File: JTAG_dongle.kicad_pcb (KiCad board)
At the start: 2 copper layers, 52.7 x 31.8 mm, 53 parts, among them J1 5V supply Enable, J2 SeggerJlink connector, J3 Conn_02x10_Odd_Even, J4 FTS-105-01-F-D

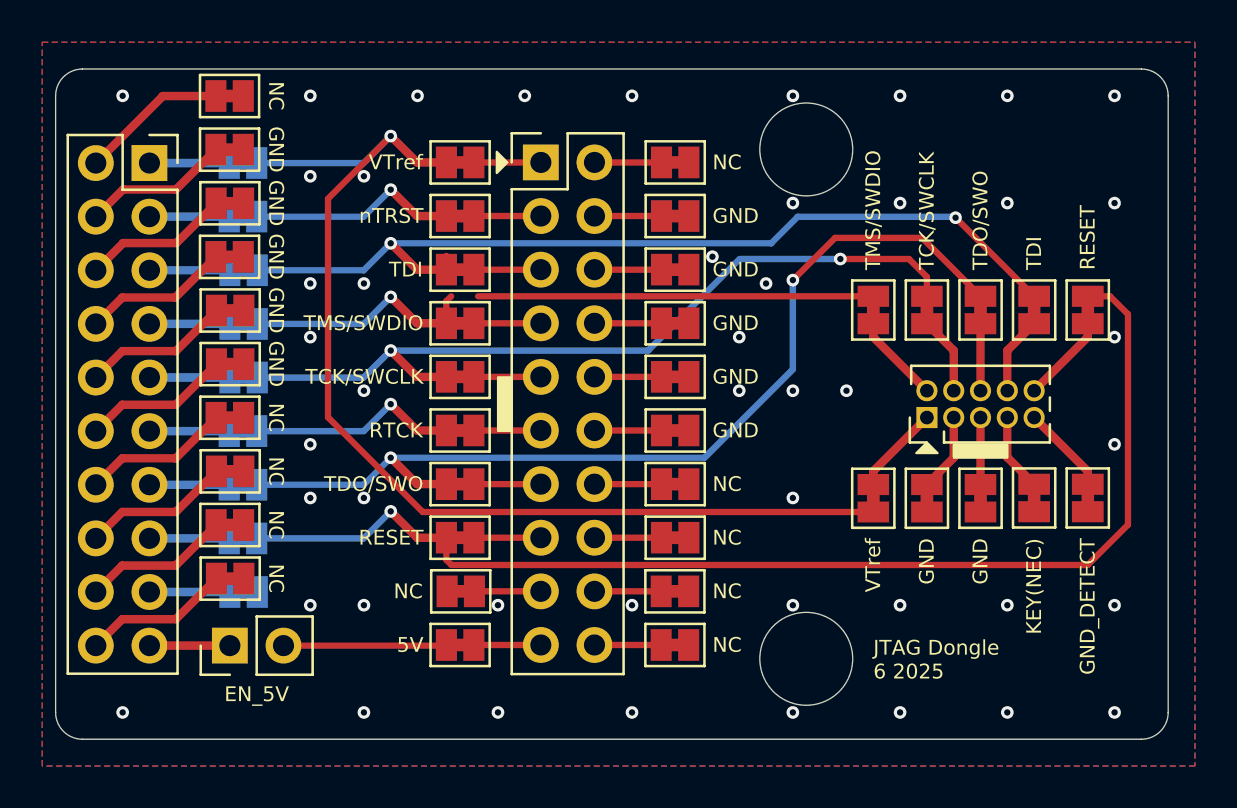
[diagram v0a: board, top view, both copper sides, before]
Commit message: fix drc erros
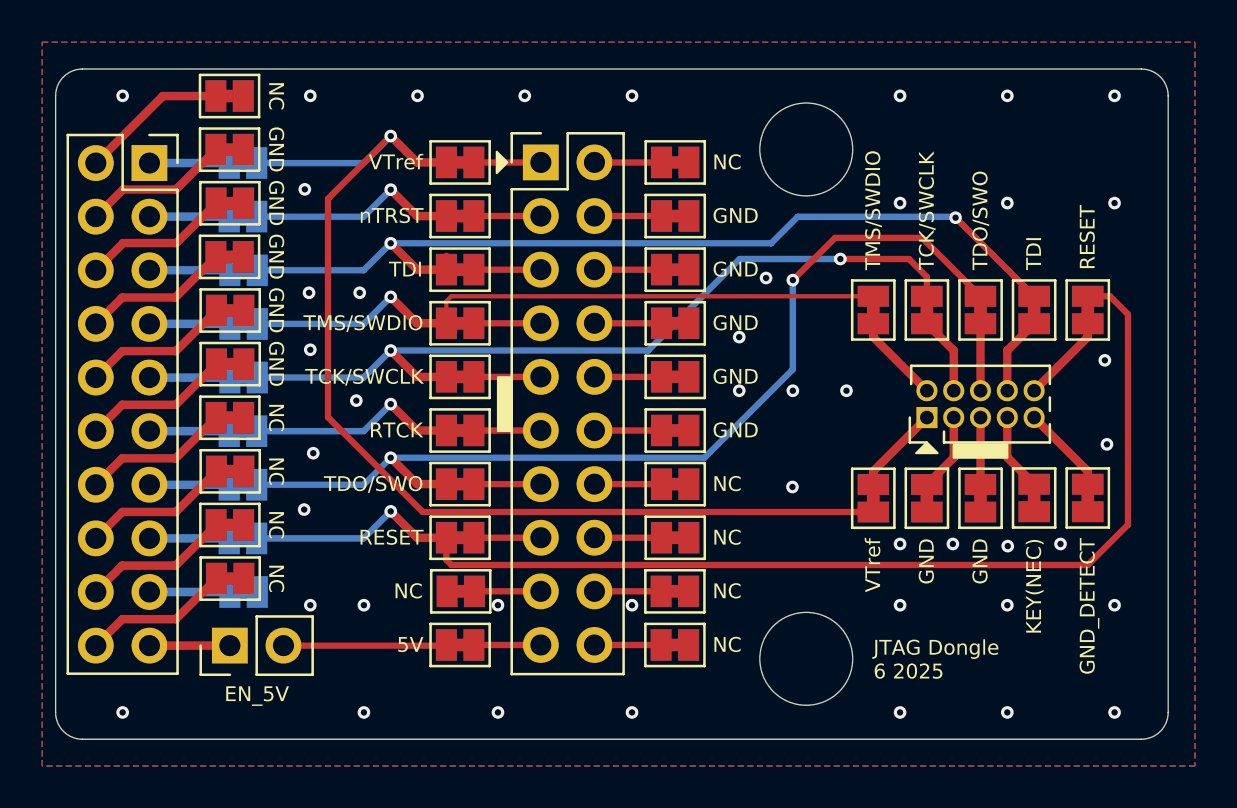
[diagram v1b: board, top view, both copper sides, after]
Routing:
- net /TMS/SWDIO: track 30.1 -> 31.4 mm
- net GND: vias 47 -> 44
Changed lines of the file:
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@@
 			(layer "F.Mask"
 				(type "Top Solder Mask")
-				(color "#000000F0")
 				(thickness 0.01)
 			)
@@
 			(layer "B.Mask"
 				(type "Bottom Solder Mask")
-				(color "#000000F0")
 				(thickness 0.01)
 			)
@@
 	)
 	(via
-		(at 83.02 51.27)
-		(size 0.6)
-		(drill 0.3)
-		(layers "F.Cu" "B.Cu")
-		(free yes)
-		(net 5)
-	)
-	(via
 		(at 93.18 56.35)
 		(size 0.6)
@@
 	)
 	(via
-		(at 83.02 75.4)
+		(at 88.1 72.5)
 		(size 0.6)
 		(drill 0.3)
@@
 	)
 	(via
-		(at 79.21 58.89)
+		(at 60.16 63.3)
 		(size 0.6)
 		(drill 0.3)
@@
 	)
 	(via
-		(at 60.16 62.7)
+		(at 98.26 51.27)
 		(size 0.6)
 		(drill 0.3)
@@
 	)
 	(via
-		(at 98.26 51.27)
+		(at 51.27 51.27)
 		(size 0.6)
 		(drill 0.3)
@@
 	)
 	(via
-		(at 51.27 51.27)
+		(at 93.18 80.48)
 		(size 0.6)
 		(drill 0.3)
@@
 	)
 	(via
-		(at 93.18 80.48)
+		(at 65.24 51.27)
 		(size 0.6)
 		(drill 0.3)
@@
 	)
 	(via
-		(at 65.24 51.27)
+		(at 62.7 75.4)
 		(size 0.6)
 		(drill 0.3)
@@
 	)
 	(via
-		(at 62.7 75.4)
+		(at 93.2 72.6)
 		(size 0.6)
 		(drill 0.3)
@@
 	)
 	(via
-		(at 81.75 60.16)
+		(at 81.75 59.9)
 		(size 0.6)
 		(drill 0.3)
@@
 	)
 	(via
-		(at 60.16 60.16)
+		(at 60.1 60.6)
 		(size 0.6)
 		(drill 0.3)
@@
 	)
 	(via
-		(at 62.7 65.24)
+		(at 62.34 65.71)
 		(size 0.6)
 		(drill 0.3)
@@
 	)
 	(via
-		(at 98.26 67.78)
+		(at 97.9 67.78)
 		(size 0.6)
 		(drill 0.3)
@@
 	)
 	(via
-		(at 98.26 56.35)
+		(at 95.7 72.5)
 		(size 0.6)
 		(drill 0.3)
@@
 	)
 	(via
-		(at 60.16 70.32)
+		(at 98.26 56.35)
 		(size 0.6)
 		(drill 0.3)
@@
 	)
 	(via
-		(at 62.7 55.08)
+		(at 59.87 70.87)
 		(size 0.6)
 		(drill 0.3)
@@
 	)
 	(via
-		(at 60.16 55.08)
+		(at 90.6 72.5)
 		(size 0.6)
 		(drill 0.3)
@@
 	)
 	(via
-		(at 62.7 60.16)
+		(at 59.9 55.7)
 		(size 0.6)
 		(drill 0.3)
@@
 	)
 	(via
-		(at 98.26 62.7)
+		(at 62.5 60.6)
 		(size 0.6)
 		(drill 0.3)
@@
 	)
 	(via
-		(at 88.1 56.35)
+		(at 97.8 63.8)
 		(size 0.6)
 		(drill 0.3)
@@
 	)
 	(via
-		(at 88.1 75.4)
+		(at 88.1 56.35)
 		(size 0.6)
 		(drill 0.3)
@@
 	)
 	(via
-		(at 80.48 62.7)
+		(at 88.1 75.4)
 		(size 0.6)
 		(drill 0.3)
@@
 	)
 	(via
-		(at 80.48 65.24)
+		(at 80.48 62.7)
 		(size 0.6)
 		(drill 0.3)
@@
 	)
 	(via
-		(at 83.02 70.32)
+		(at 80.48 65.24)
 		(size 0.6)
 		(drill 0.3)
@@
 	)
 	(via
-		(at 83.02 56.35)
+		(at 83 69.8)
 		(size 0.6)
 		(drill 0.3)
@@
 	)
 	(via
-		(at 83.02 80.48)
-		(size 0.6)
-		(drill 0.3)
-		(layers "F.Cu" "B.Cu")
-		(free yes)
-		(net 5)
-	)
-	(via
 		(at 51.27 80.48)
 		(size 0.6)
@@
 	)
 	(via
-		(at 60.16 67.78)
+		(at 60.3 68.2)
 		(size 0.6)
 		(drill 0.3)
@@
 		(net 5)
 	)
-	(via
-		(at 62.7 70.32)
-		(size 0.6)
-		(drill 0.3)
-		(layers "F.Cu" "B.Cu")
-		(free yes)
-		(net 5)
-	)
 	(segment
 		(start 65.2195 67.1245)
@@
 	)
 	(segment
-		(start 86.83 60.765)
-		(end 68.1065 60.765)
-		(width 0.3)
-		(layer "F.Cu")
-		(net 11)
-	)
-	(segment
 		(start 66.8365 60.765)
-		(end 66.607 60.9945)
-		(width 0.3)
+		(end 86.83 60.765)
+		(width 0.2)
 		(layer "F.Cu")
 		(net 11)
 	)
 	(segment
-		(start 66.607 60.9945)
-		(end 66.607 62.0445)
-		(width 0.3)
+		(start 66.607 62.0445)
+		(end 66.607 60.9945)
+		(width 0.2)
 		(layer "F.Cu")
 		(net 11)
@@
 		(layer "F.Cu")
 		(net 11)
+	)
+	(segment
+		(start 66.607 60.9945)
+		(end 66.8365 60.765)
+		(width 0.2)
+		(layer "F.Cu")
+		(net 11)

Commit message: add drawing
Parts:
- added G***: LOGO, LOGO, B.Cu at (94.0, 56.0)
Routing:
- net GND: vias 44 -> 40
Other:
- board text added: "JTAG Dongle 06 2025"
- board text removed: "JTAG Dongle 6 2025"
